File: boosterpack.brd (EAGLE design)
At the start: 75.2 x 55.9 mm, 38 parts, among them J1 POWERPOLE_DOUBLE, J2 PHOENIXSCREWTERMINAL_2, J3 PHOENIXSCREWTERMINAL_2

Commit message: moved a resistor that was bothering me
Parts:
- moved R5 1.91 mm to (32.4, 33.0)
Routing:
- net +3V3: track 133.6 -> 131.5 mm
- net N$22: track 29.5 -> 28.7 mm
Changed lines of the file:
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@@
 <element name="C5" library="resistor" package="C025-025X050" value="0.1uF" x="43.815" y="45.72"/>
 <element name="C6" library="resistor" package="C025-025X050" value="" x="64.135" y="52.07" rot="R270"/>
-<element name="R5" library="resistor" package="0204/5" value="5k" x="32.385" y="31.115" rot="R90"/>
+<element name="R5" library="resistor" package="0204/5" value="5k" x="32.385" y="33.02" rot="R90"/>
 <element name="C7" library="resistor" package="C025-024X044" value="0.22uF" x="59.055" y="43.815"/>
 </elements>
@@
 <contactref element="U$3" pad="23"/>
 <contactref element="R5" pad="2"/>
-<wire x1="32.385" y1="33.655" x2="34.29" y2="35.56" width="0.6096" layer="16"/>
-<wire x1="34.29" y1="35.56" x2="58.42" y2="35.56" width="0.6096" layer="16"/>
+<wire x1="32.385" y1="35.56" x2="58.42" y2="35.56" width="0.6096" layer="16"/>
 <wire x1="58.42" y1="35.56" x2="60.325" y2="33.655" width="0.6096" layer="16"/>
 </signal>
@@
 <wire x1="17.78" y1="69.215" x2="19.431" y2="69.215" width="0.6096" layer="1"/>
 <wire x1="19.431" y1="69.215" x2="19.685" y2="69.469" width="0.6096" layer="1"/>
-<wire x1="32.385" y1="28.575" x2="36.195" y2="32.385" width="0.6096" layer="1"/>
-<wire x1="34.925" y1="33.655" x2="36.195" y2="32.385" width="0.6096" layer="1"/>
-<wire x1="36.195" y1="32.385" x2="38.735" y2="32.385" width="0.6096" layer="1"/>
+<wire x1="34.925" y1="33.655" x2="34.925" y2="32.385" width="0.6096" layer="1"/>
+<wire x1="34.925" y1="32.385" x2="38.735" y2="32.385" width="0.6096" layer="1"/>
 <wire x1="38.735" y1="32.385" x2="40.005" y2="33.655" width="0.6096" layer="1"/>
 <wire x1="40.005" y1="33.655" x2="40.64" y2="33.655" width="0.6096" layer="1"/>
 <wire x1="12.065" y1="45.085" x2="22.225" y2="34.925" width="0.6096" layer="1"/>
-<wire x1="22.225" y1="34.925" x2="26.035" y2="34.925" width="0.6096" layer="1"/>
-<wire x1="26.035" y1="34.925" x2="32.385" y2="28.575" width="0.6096" layer="1"/>
+<wire x1="22.225" y1="34.925" x2="27.94" y2="34.925" width="0.6096" layer="1"/>
+<wire x1="27.94" y1="34.925" x2="32.385" y2="30.48" width="0.6096" layer="1"/>
+<wire x1="32.385" y1="30.48" x2="33.02" y2="30.48" width="0.6096" layer="1"/>
+<wire x1="33.02" y1="30.48" x2="34.925" y2="32.385" width="0.6096" layer="1"/>
 </signal>
 <signal name="N$14">

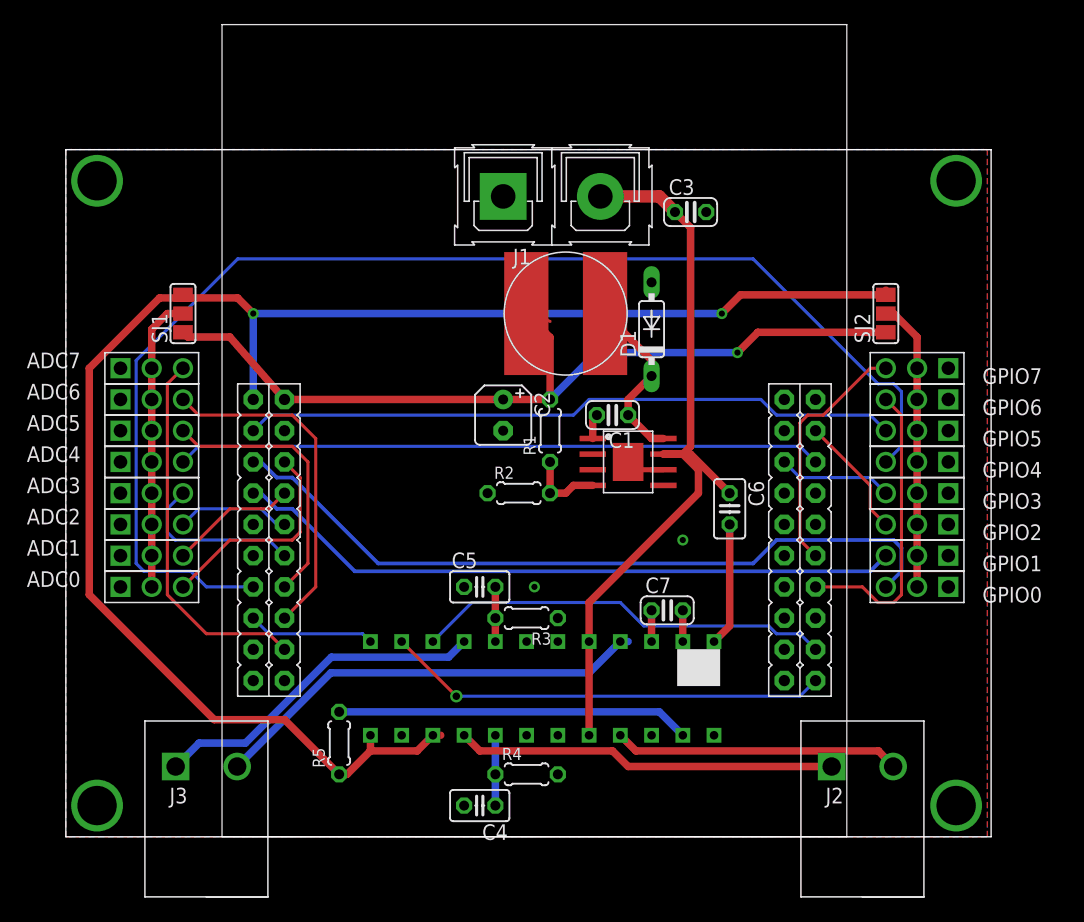
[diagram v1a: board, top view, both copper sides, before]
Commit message: shrank the board; added decopling cap for power
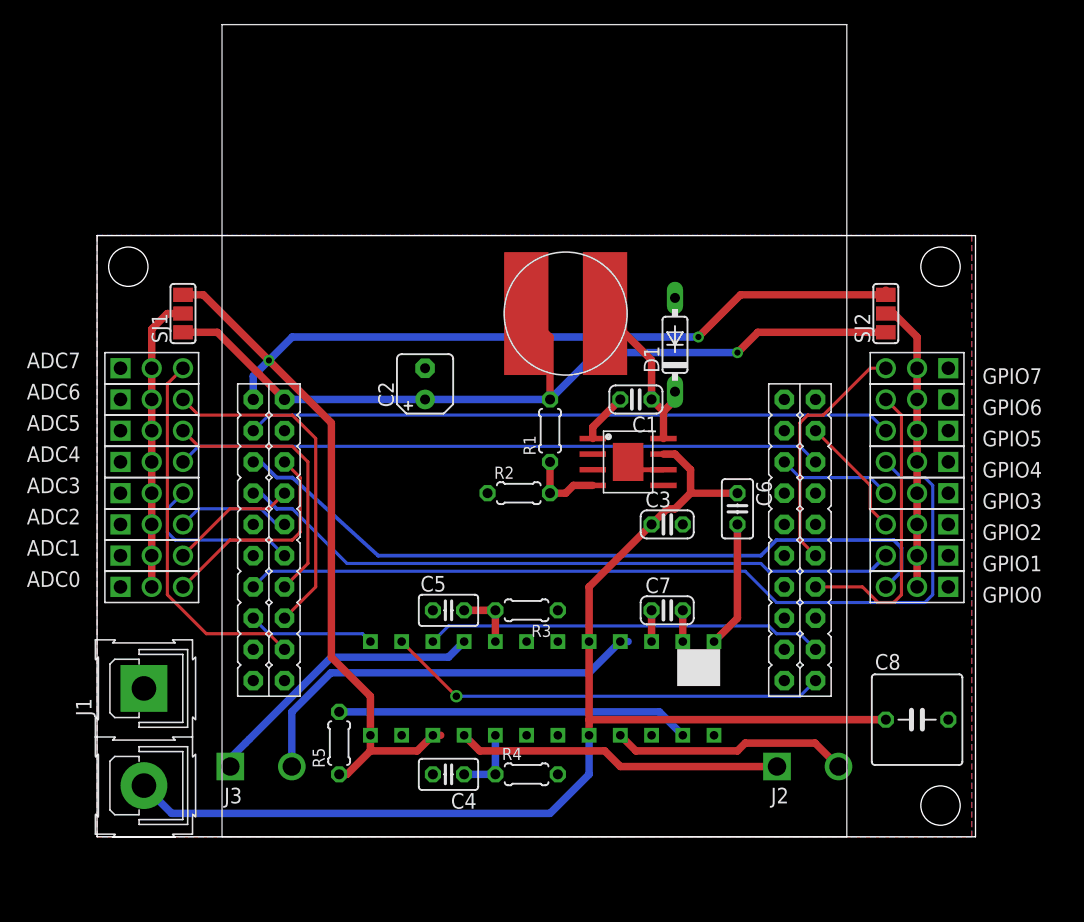
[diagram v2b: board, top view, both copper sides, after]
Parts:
- added C8: 16V, resistor:C050-075X075
- moved J1 49.5 mm to (16.5, 37.5), turned to 270 degrees
- moved C3 25.5 mm to (59.1, 50.8)
- moved C2 6.84 mm to (39.4, 62.2), turned to 90 degrees
- moved J2 4.45 mm to (70.5, 31.1)
- moved J3 4.45 mm to (26.0, 31.1)
- moved C4 3.59 mm to (41.3, 30.5)
- moved C5 3.18 mm to (41.3, 43.8)
- moved C1 2.29 mm to (56.5, 61.0)
- moved D1 2.29 mm to (59.7, 65.4)
- moved R3 0.63 mm to (47.6, 43.8)
- moved C6 0.63 mm to (64.8, 52.1)
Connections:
- net CP2 renamed N$23
- net GND: now also C8.2
- net VCC: now also C8.1
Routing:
- net VCC: track 62.4 -> 97.7 mm
- net N$2: track 103.2 -> 70.6 mm
- net +3V3: track 131.5 -> 110.7 mm
- net N$17: track 30.9 -> 26.5 mm
- net N$15: track 27.7 -> 23.6 mm
- net N$18: track 23.3 -> 19.3 mm
- net +5V: track 72.3 -> 70.1 mm
- net N$9: track 2.04 -> 4.10 mm
- net N$14: track 36.0 -> 34.2 mm
- net MOTORFSS: track 34.0 -> 32.4 mm
- net N$3: track 53.5 -> 52.5 mm
- net GPIO0: track 60.9 -> 60.2 mm
- net N$19: track 4.45 -> 5.08 mm
- net GND: vias 2 -> 0
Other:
- board size 75.2 x 55.9 mm -> 71.4 x 48.9 mm
- board text removed: "0"
- board text removed: "1"
- board text removed: "2"
- board text removed: "3"
- board text removed: "3V3"
- board text removed: "4"
- board text removed: "5"
- board text removed: "5V"
- board text removed: "6"
- board text removed: "7"
- board text removed: "Ground"
- board text removed: "Port B"
- board text removed: "Port D"
- board text removed: "Port E"
- board text removed: "Power"
- board text removed: "Signal"

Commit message: had @cmonr look at it; implemented suggestions
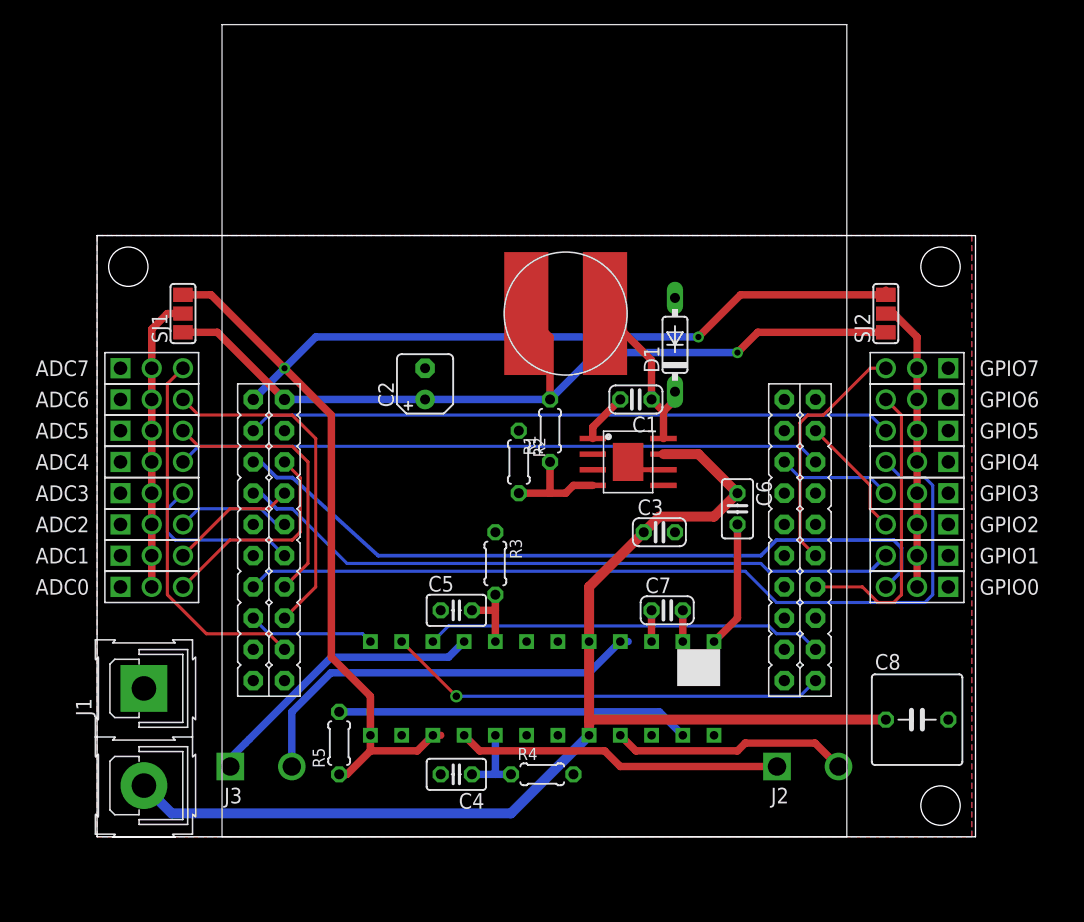
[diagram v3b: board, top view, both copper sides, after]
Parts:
- moved R3 4.58 mm to (45.1, 47.6), turned to 270 degrees
- moved R2 2.54 mm to (47.0, 55.9), turned to 270 degrees
- moved R4 1.27 mm to (48.9, 30.5)
- moved C3 0.90 mm to (58.4, 50.2)
- moved C4 0.63 mm to (41.9, 30.5)
- moved C5 0.63 mm to (41.9, 43.8)
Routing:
- net N$10: track 6.28 -> 8.82 mm
- net VCC: track 97.7 -> 98.5 mm
- net +3V3: track 110.7 -> 110.0 mm
- net N$19: track 5.08 -> 5.72 mm
- net N$20: track 5.71 -> 6.35 mm
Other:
- board text added: "0"
- board text added: "1"
- board text added: "2"
- board text added: "3"
- board text added: "3v3"
- board text added: "4"
- board text added: "5"
- board text added: "5v"
- board text added: "6"
- board text added: "7"
- board text added: "Ground"
- board text added: "Port B"
- board text added: "Port D"
- board text added: "Port E"
- board text added: "Power"
- board text added: "Signal"

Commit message: tidied up gerbers
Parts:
- moved L1 9.25 mm to (41.9, 65.4)
- moved C2 5.71 mm to (33.7, 62.2)
- moved J1 2.54 mm to (16.5, 40.0)
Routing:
- net N$11: track 14.1 -> 20.1 mm
- net +5V: track 70.1 -> 69.2 mm
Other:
- board size 71.4 x 48.9 mm -> 71.4 x 44.4 mm
